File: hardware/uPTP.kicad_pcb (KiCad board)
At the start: 2 copper layers, 30 x 30 mm, 2 parts, among them U1 CH32V307WCU6, U2 HC-RJ45-055-7

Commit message: Some more handy components
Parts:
- added D1: USBLC6-2SC6, uPTP:SOT-23-6_L2.9-W1.6-P0.95-LS2.8-BL, F.Cu at (156.1, 119.0)
- added USB1: TYPE-C 16PIN 2MD(073), uPTP:USB-C-SMD_TYPE-C-16PIN, F.Cu at (156.0, 126.0)
- moved U2 1.00 mm to (140.0, 122.0)
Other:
- board size 30 x 30 mm -> 33 x 30 mm

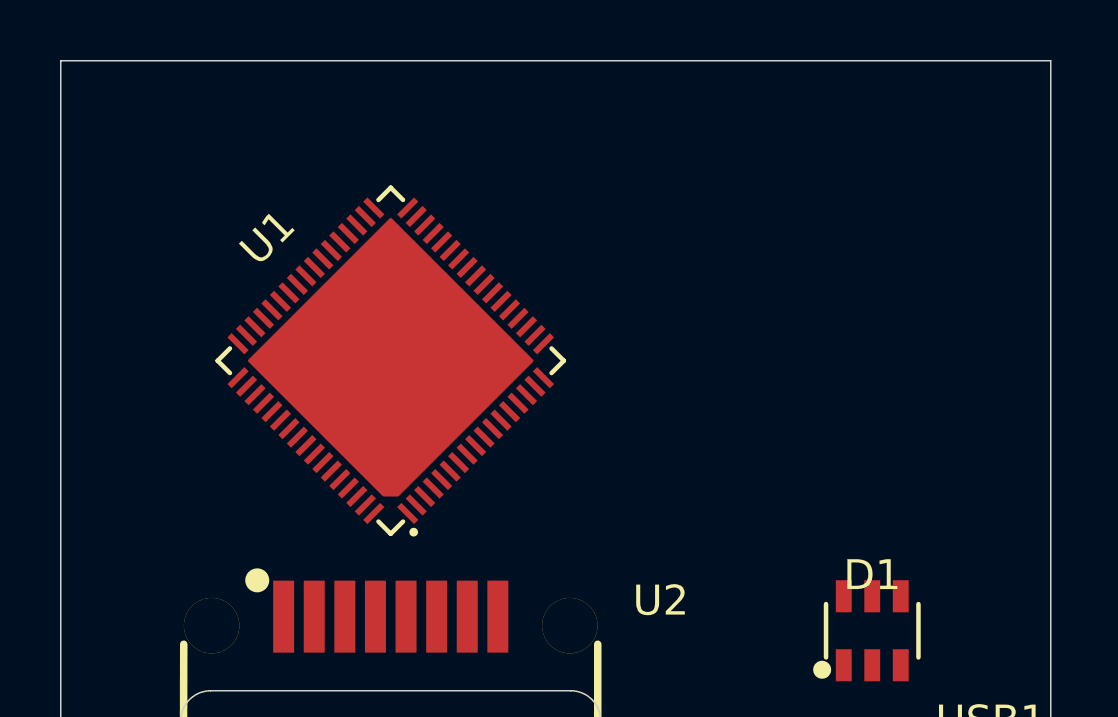
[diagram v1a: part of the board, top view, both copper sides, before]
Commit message: Add magnetics
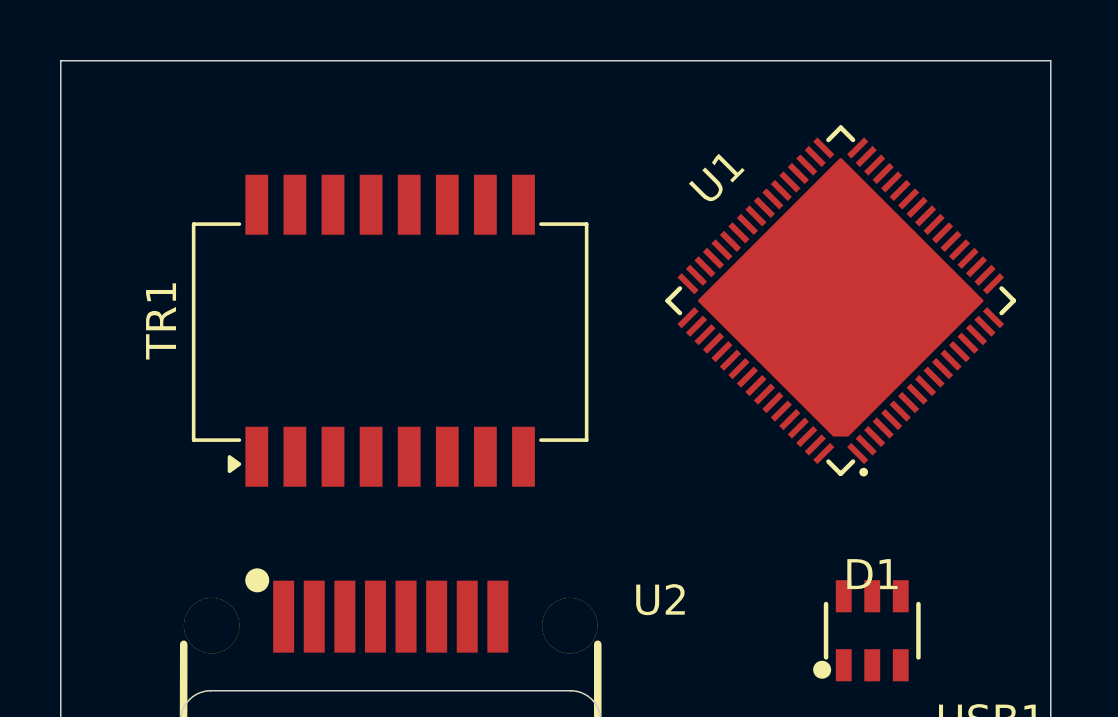
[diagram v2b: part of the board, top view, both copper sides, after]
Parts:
- added TR1: ~, uPTP:B1608S, F.Cu at (140.0, 109.0)
- moved U1 15.1 mm to (155.0, 108.0)

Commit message: Nice first render
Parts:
- added H1: MountingHole_Pad, MountingHole:MountingHole_3.2mm_M3_Pad, F.Cu at (161.0, 110.0)
- added H2: MountingHole_Pad, MountingHole:MountingHole_3.2mm_M3_Pad, F.Cu at (134.0, 94.0)
- added J1: Conn_01x04_Pin, Connector_PinHeader_2.54mm:PinHeader_1x04_P2.54mm_Horizontal, F.Cu at (140.2, 93.4)
- moved U1 7.28 mm to (153.0, 101.0)
- moved USB1 2.00 mm to (158.0, 126.0)
- moved D1 1.95 mm to (158.0, 119.0)
- moved TR1 1.41 mm to (141.0, 110.0)
- moved U2 1.00 mm to (141.0, 122.0)
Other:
- board size 33 x 30 mm -> 35 x 40 mm

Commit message: POE CTRL?
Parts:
- added U3: TMI7301, uPTP:SOP-8_L4.9-W3.9-P1.27-LS6.0-TL, F.Cu at (151.1, 112.9)

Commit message: Backup progress
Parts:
- removed U3: TMI7301, uPTP:SOP-8_L4.9-W3.9-P1.27-LS6.0-TL
- added C2: 100n, Capacitor_SMD:C_0402_1005Metric, F.Cu at (204.4, 104.4)
- added C3: 100n, Capacitor_SMD:C_0402_1005Metric, F.Cu at (204.4, 106.4)
- added C4: 100n, Capacitor_SMD:C_0402_1005Metric, F.Cu at (187.2, 106.5)
- added D1: D_Schottky, Diode_SMD:D_SOD-323, F.Cu at (187.9, 104.1)
- added D3: MB2S, Package_TO_SOT_SMD:TO-269AA, F.Cu at (195.5, 121.9)
- added D4: MB2S, Package_TO_SOT_SMD:TO-269AA, F.Cu at (195.5, 128.3)
- added D5: D_Schottky, Diode_SMD:D_SOD-323, F.Cu at (186.0, 121.0)
- added J4: HC-RJ45-055-7, uPTP:RJ45-SMD_HC-RJ45-055-7_1, F.Cu at (141.0, 121.9)
- added R1: 5.1k, Resistor_SMD:R_0402_1005Metric, F.Cu at (211.8, 104.4)
- added R2: 5.1k, Resistor_SMD:R_0402_1005Metric, F.Cu at (211.8, 106.4)
- added R3: 75, Resistor_SMD:R_0402_1005Metric, F.Cu at (201.6, 104.4)
- added R4: 75, Resistor_SMD:R_0402_1005Metric, F.Cu at (201.6, 106.4)
- added R5: 75, Resistor_SMD:R_0402_1005Metric, F.Cu at (201.6, 108.4)
- added R6: 75, Resistor_SMD:R_0402_1005Metric, F.Cu at (201.6, 110.4)
- U2: value HC-RJ45-055-7 -> TMI7301; footprint uPTP:RJ45-SMD_HC-RJ45-055-7_1 -> uPTP:SOP-8_L4.9-W3.9-P1.27-LS6.0-TL
- moved U2 64.0 mm to (205.0, 122.0)
- moved H1 16.0 mm to (161.0, 94.0)
- moved D2 1.00 mm to (158.0, 120.0)
- turned TR1 to -90 degrees
- renumbered D1 to D2
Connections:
- D2 pad 1: unconnected-(D1-Pad1) -> /USB_D_CONN_N
- D2 pad 2: unconnected-(D1-Pad2) -> GND
- D2 pad 3: unconnected-(D1-Pad3) -> /USB_D_CONN_P
- D2 pad 4: unconnected-(D1-Pad4) -> /USB_D_P
- D2 pad 5: unconnected-(D1-Pad5) -> Net-(D2-VBUS)
- D2 pad 6: unconnected-(D1-Pad6) -> /USB_D_N
- TR1 pad 1: unconnected-(TR1-TD+-Pad1) -> /Ethernet and POE/ETH_D_TX_P
- TR1 pad 10: unconnected-(TR1-C_RX-Pad10) -> Net-(TR1-C_RX)
- TR1 pad 11: unconnected-(TR1-RX+-Pad11) -> /Ethernet and POE/ETH_D_ISO_RX_P
- TR1 pad 14: unconnected-(TR1-TX--Pad14) -> /Ethernet and POE/ETH_D_ISO_TX_N
- TR1 pad 15: unconnected-(TR1-C_TX-Pad15) -> Net-(TR1-C_TX)
- TR1 pad 16: unconnected-(TR1-TX+-Pad16) -> /Ethernet and POE/ETH_D_ISO_TX_P
- TR1 pad 2: unconnected-(TR1-C_TD-Pad2) -> +3V3
- TR1 pad 3: unconnected-(TR1-TD--Pad3) -> /Ethernet and POE/ETH_D_TX_N
- TR1 pad 6: unconnected-(TR1-RD+-Pad6) -> /Ethernet and POE/ETH_D_RX_P
- TR1 pad 7: unconnected-(TR1-C_RD-Pad7) -> +3V3
- TR1 pad 8: unconnected-(TR1-RD--Pad8) -> /Ethernet and POE/ETH_D_RX_N
- TR1 pad 9: unconnected-(TR1-RX--Pad9) -> /Ethernet and POE/ETH_D_ISO_RX_N
- USB1 pad 1: unconnected-(USB1-GND-Pad1) -> GND
- USB1 pad 10: unconnected-(USB1-CC2-Pad10) -> Net-(USB1-CC2)
- USB1 pad 11: unconnected-(USB1-VBUS-Pad11) -> +5V_USB
- USB1 pad 12: unconnected-(USB1-GND-Pad12) -> GND
- USB1 pad 13: unconnected-(USB1-SHELL-Pad13) -> GND
- USB1 pad 2: unconnected-(USB1-VBUS-Pad2) -> +5V_USB
- USB1 pad 4: unconnected-(USB1-CC1-Pad4) -> Net-(USB1-CC1)
- USB1 pad 5: unconnected-(USB1-DN2-Pad5) -> /USB_D_CONN_N
- USB1 pad 6: unconnected-(USB1-DP1-Pad6) -> /USB_D_CONN_P
- USB1 pad 7: unconnected-(USB1-DN1-Pad7) -> /USB_D_CONN_N
- USB1 pad 8: unconnected-(USB1-DP2-Pad8) -> /USB_D_CONN_P

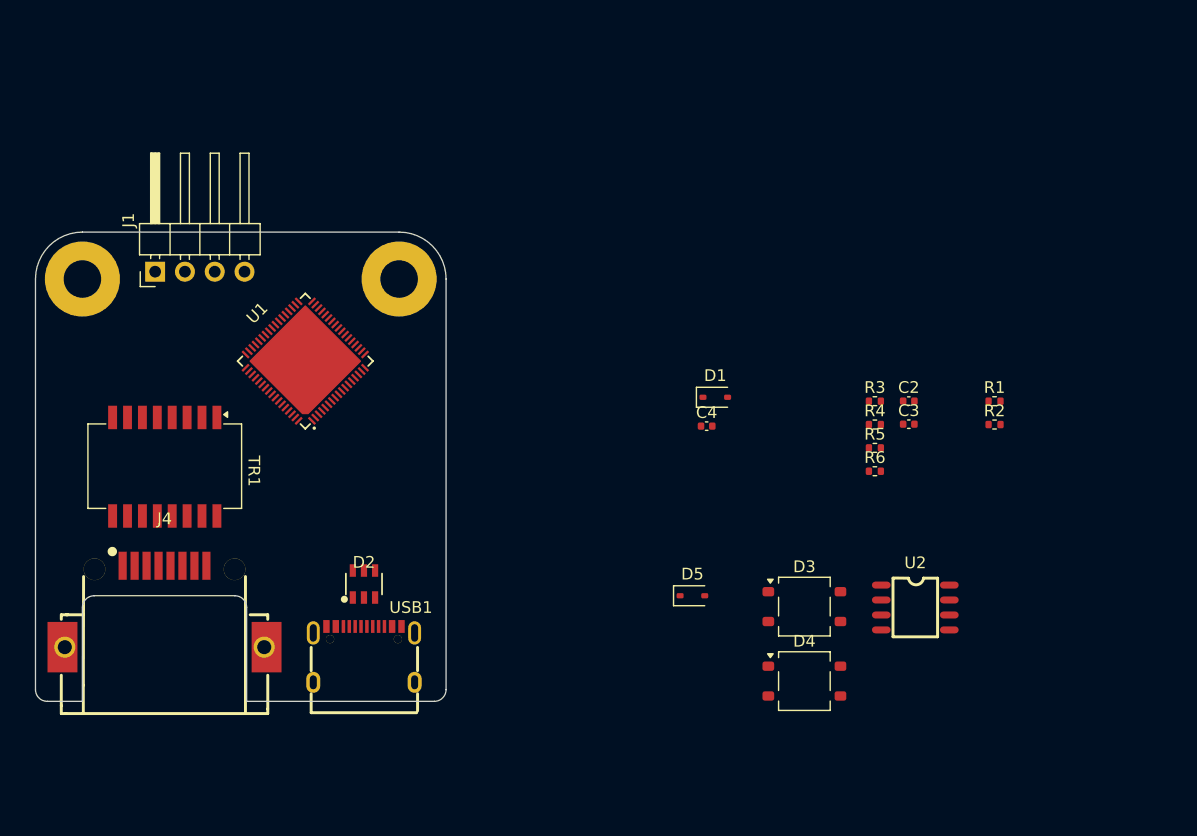
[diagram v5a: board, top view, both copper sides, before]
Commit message: POE layout considerationa
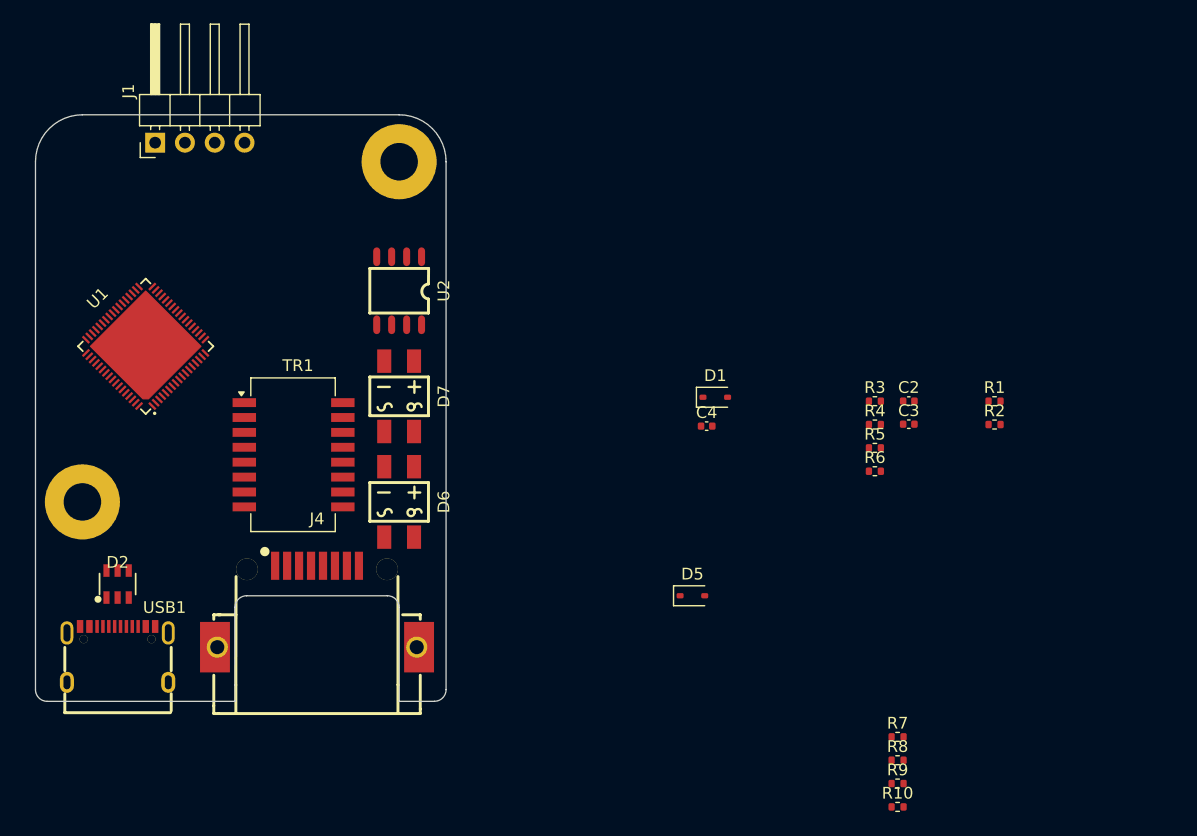
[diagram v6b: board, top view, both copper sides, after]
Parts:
- removed D3, D4: MB2S, Package_TO_SOT_SMD:TO-269AA
- added D6: MB10F_C2491, uPTP:DIO-BG-SMD_4P-L4.9-W4.0-P2.54-LS7.0-BR, F.Cu at (161.0, 113.0)
- added D7: MB10F_C2491, uPTP:DIO-BG-SMD_4P-L4.9-W4.0-P2.54-LS7.0-BR, F.Cu at (161.0, 104.0)
- added R10: 49.9, Resistor_SMD:R_0402_1005Metric, F.Cu at (203.5, 139.0)
- added R7: 49.9, Resistor_SMD:R_0402_1005Metric, F.Cu at (203.5, 133.0)
- added R8: 49.9, Resistor_SMD:R_0402_1005Metric, F.Cu at (203.5, 135.0)
- added R9: 49.9, Resistor_SMD:R_0402_1005Metric, F.Cu at (203.5, 137.0)
- moved U2 51.6 mm to (161.0, 95.0), turned to -90 degrees
- moved D2 21.0 mm to (137.0, 120.0)
- moved USB1 21.0 mm to (137.0, 126.0)
- moved H2 19.0 mm to (134.0, 113.0)
- moved U1 13.7 mm to (139.4, 99.7)
- moved J4 13.0 mm to (154.0, 121.9)
- moved TR1 11.0 mm to (152.0, 109.0), turned to 0 degrees
- moved J1 11.0 mm to (140.2, 82.4)
- moved H1 10.0 mm to (161.0, 84.0)
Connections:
- net Net-(TR1-C_RX) renamed /Ethernet and POE/ETH_RX1
- net Net-(TR1-C_TX) renamed /Ethernet and POE/ETH_TX1
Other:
- board size 35 x 40 mm -> 35 x 50 mm

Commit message: Vaguely convincing render...
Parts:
- removed the R10 at (203.5, 139.0)
- removed the R7 at (203.5, 133.0)
- removed the R8 at (203.5, 135.0)
- removed the R9 at (203.5, 137.0)
- added C5: 100n 100V/60V?, Capacitor_SMD:C_0805_2012Metric, F.Cu at (161.0, 95.5)
- added D5: SMAJ58A, Diode_SMD:D_SMA, F.Cu at (161.0, 98.5)
- added J2: PPS_UFL, uPTP:IPEX-SMD_HC-RF-IPEX0303-01, F.Cu at (137.0, 87.0)
- added J3: PPS_SMA, Connector_Coaxial:SMA_Samtec_SMA-J-P-H-ST-EM1_EdgeMount, F.Cu at (137.0, 82.0)
- added JP1: POE_ENABLE, Jumper:SolderJumper-2_P1.3mm_Bridged_RoundedPad1.0x1.5mm, F.Cu at (225.3, 115.0)
- added JP2: SHIELD_BRIDGE, Jumper:SolderJumper-2_P1.3mm_Open_RoundedPad1.0x1.5mm, B.Cu at (161.5, 116.3)
- added R11: 24.9k, Resistor_SMD:R_0402_1005Metric, F.Cu at (164.0, 92.5)
- added R12: 1k, Resistor_SMD:R_0402_1005Metric, F.Cu at (162.5, 92.5)
- added R13: 49.9, Resistor_SMD:R_0402_1005Metric, F.Cu at (199.5, 108.5)
- added R14: 49.9, Resistor_SMD:R_0402_1005Metric, F.Cu at (199.5, 110.5)
- added R15: 49.9, Resistor_SMD:R_0402_1005Metric, F.Cu at (199.5, 112.5)
- added R16: 100k, Resistor_SMD:R_0402_1005Metric, F.Cu at (153.0, 92.0)
- added R17: 49.9, Resistor_SMD:R_0402_1005Metric, F.Cu at (199.5, 116.5)
- moved C4 60.7 mm to (144.0, 112.0), turned to 180 degrees
- moved C3 60.5 mm to (144.0, 107.0)
- moved R8 55.0 mm to (154.0, 134.0), turned to 90 degrees
- moved R9 52.3 mm to (156.0, 134.0), turned to 90 degrees
- moved R10 49.6 mm to (158.0, 134.0), turned to 90 degrees
- moved R7 44.1 mm to (157.5, 106.5), turned to 90 degrees
- moved U2 5.00 mm to (158.0, 91.0), turned to 180 degrees
- moved U1 3.07 mm to (138.0, 97.0)
- moved J1 3.00 mm to (143.2, 82.4)
- moved TR1 1.00 mm to (151.0, 109.0)
- moved D4 0.50 mm to (161.0, 104.5)
- renumbered C4 to C1, C2 to C3, C3 to C4, D6 to D3, D7 to D4, D5 to D6, R6 to R10, R3 to R7, R4 to R8, R5 to R9
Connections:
- net Net-(C1-Pad1) renamed /Ethernet and POE/ETH_BOB_SMITH
- C1 pad 2: Net-(D2-VBUS) -> GND
- D2 pad 5: Net-(D2-VBUS) -> +5V_USB
- D3 pad 1: Net-(D6-+) -> /Ethernet and POE/ETH_POE_P
- D3 pad 3: Net-(D6--) -> /Ethernet and POE/ETH_POE_N
- D4 pad 1: Net-(D6-+) -> /Ethernet and POE/ETH_POE_P
- D4 pad 3: Net-(D6--) -> /Ethernet and POE/ETH_POE_N
- D6 pad 1: unconnected-(D5-K-Pad1) -> /Ethernet and POE/V_POE
- D6 pad 2: unconnected-(D5-A-Pad2) -> /Ethernet and POE/ETH_POE_P
- U2 pad 1: unconnected-(U2-MODE-Pad1) -> /Ethernet and POE/ETH_POE_N
- U2 pad 2: unconnected-(U2-CLASS-Pad2) -> /Ethernet and POE/ETH_POE_CLASS
- U2 pad 3: unconnected-(U2-DET-Pad3) -> /Ethernet and POE/ETH_POE_DET
- U2 pad 4: unconnected-(U2-VSS-Pad4) -> /Ethernet and POE/ETH_POE_N
- U2 pad 5: unconnected-(U2-RTN-Pad5) -> GND
- U2 pad 6: unconnected-(U2-PGN_MPS-Pad6) -> /Ethernet and POE/POE_READY
- U2 pad 8: unconnected-(U2-VDD-Pad8) -> /Ethernet and POE/ETH_POE_P
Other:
- outline, holes or cut-outs redrawn

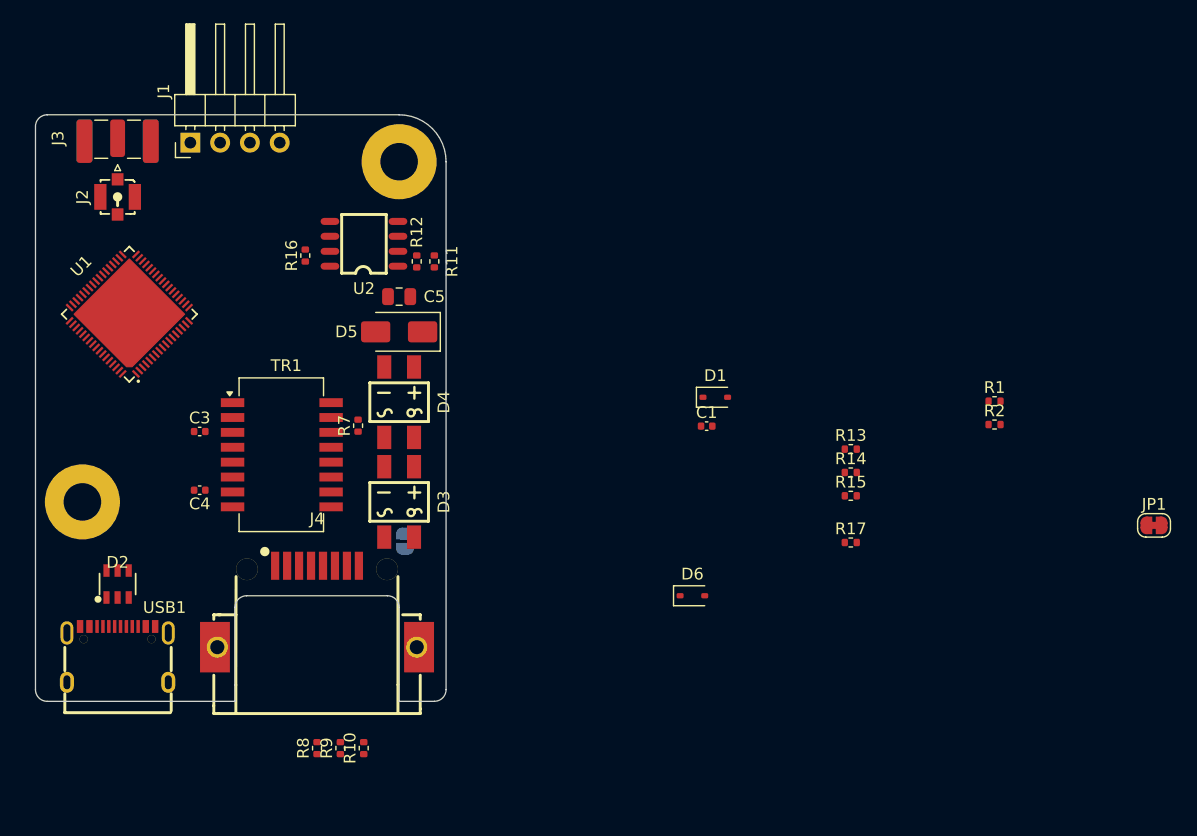
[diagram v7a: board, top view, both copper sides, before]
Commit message: Component selection mostly done
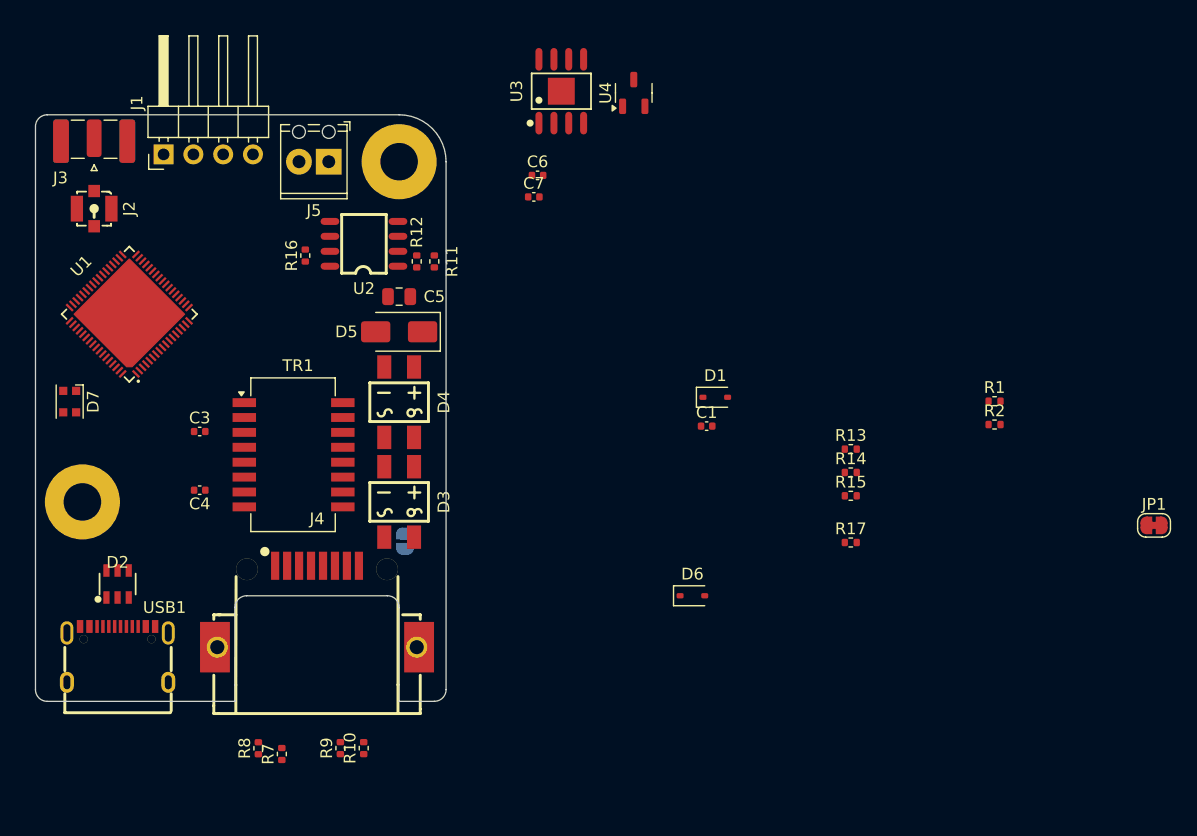
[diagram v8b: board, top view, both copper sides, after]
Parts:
- added C6: 20p, Capacitor_SMD:C_0402_1005Metric, F.Cu at (172.8, 85.2)
- added C7: 20p, Capacitor_SMD:C_0402_1005Metric, F.Cu at (172.5, 87.0)
- added D7: WS2812B-2020, LED_SMD:LED_WS2812B-2020_PLCC4_2.0x2.0mm, F.Cu at (132.9, 104.5)
- added J5: AUX_PWR, TerminalBlock_Phoenix:TerminalBlock_Phoenix_MPT-0,5-2-2.54_1x02_P2.54mm_Horizontal, F.Cu at (155.0, 84.0)
- added U3: LMR16030SDDAR, uPTP:SOIC-8_L4.9-W3.9-P1.27-LS6.0-BL-EP2.3, F.Cu at (174.8, 78.0)
- added U4: XC6206P332MR-G, Package_TO_SOT_SMD:SOT-23-3, F.Cu at (181.0, 78.1)
- moved R7 28.7 mm to (151.0, 134.5)
- moved R8 5.00 mm to (149.0, 134.0)
- moved J1 2.49 mm to (140.9, 83.4)
- moved J2 2.24 mm to (135.0, 88.0)
- moved J3 2.00 mm to (135.0, 82.0)
- moved TR1 1.00 mm to (152.0, 109.0)
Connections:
- J2 pad 1: unconnected-(J2-In-Pad1) -> /PPS_OUT
- J2 pad 2: unconnected-(J2-Ext-Pad2) -> GND
- J3 pad 1: unconnected-(J3-In-Pad1) -> /PPS_OUT
- J3 pad 2: unconnected-(J3-Ext-Pad2) -> GND
